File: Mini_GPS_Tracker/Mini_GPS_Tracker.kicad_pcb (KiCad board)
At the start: 4 copper layers, 38.1 x 99.1 mm, 56 parts, among them J1 USB_C_Receptacle, J2 Screw_Terminal_01x02, J3 901-10512-1, J4 Conn_ARM_JTAG_SWD_10, SW1 SW_Push, SW2 MLL1200S, U1 CH340E, U2 MS5611-01BA, U3 LD1117S33TR_SOT223, U4 MAX-8Q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

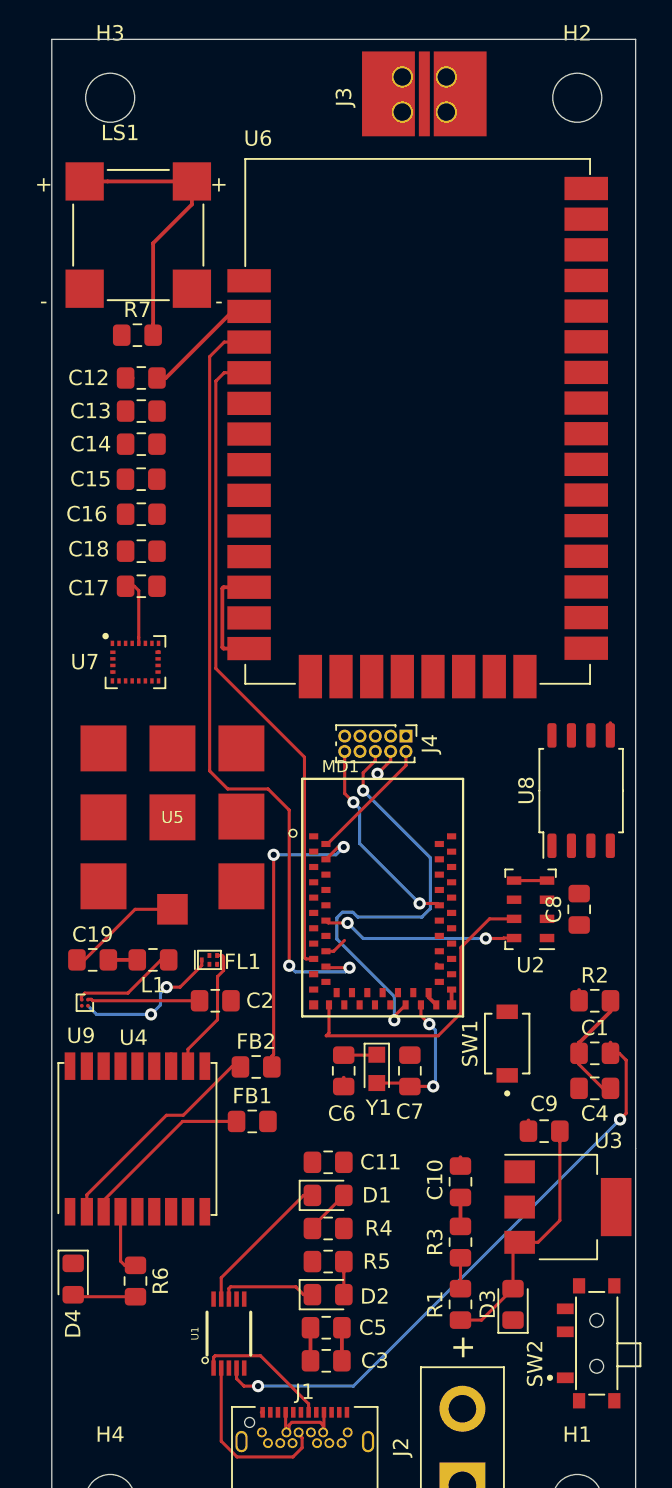
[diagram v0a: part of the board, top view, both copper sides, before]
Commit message: all  artemis connections routed
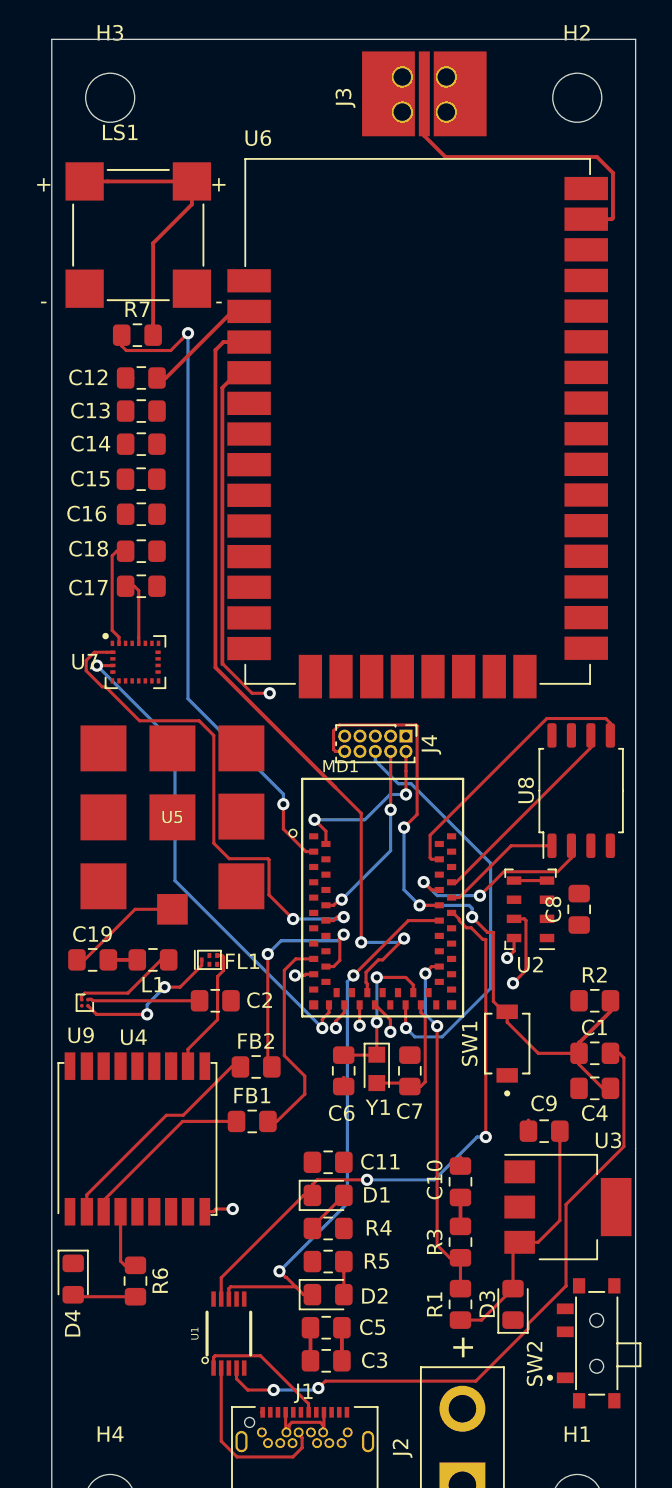
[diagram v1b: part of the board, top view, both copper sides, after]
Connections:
- MD1 pad 11: cs_flash -> Net-(MD1-Pad11)
- MD1 pad 12: Pressure_SCL -> 9_SCL
- MD1 pad 13: clk_flash -> Net-(MD1-Pad13)
- MD1 pad 16: buzzer -> Net-(MD1-Pad16)
- MD1 pad 17: TRANS_RX -> GPS_RX
- MD1 pad 18: TRANS_TX -> GPS_TX
- MD1 pad 19: Net-(MD1-Pad19) -> Pressure_SCL
- MD1 pad 23: Pressure_SDA -> 9_SDA
- MD1 pad 25: Net-(MD1-Pad25) -> Pressure_SDA
- MD1 pad 27: Net-(MD1-Pad27) -> TRANS_RX
- MD1 pad 28: Net-(MD1-Pad28) -> TRANS_TX
- MD1 pad 29: Net-(MD1-Pad29) -> gps_reset
- MD1 pad 3: Net-(MD1-Pad3) -> buzzer
- MD1 pad 4: GPS_TX -> Net-(MD1-Pad4)
- MD1 pad 51: Net-(MD1-Pad51) -> cs_flash
- MD1 pad 52: 9_SDA -> MISO_Flash
- MD1 pad 53: 9_SCL -> clk_flash
- MD1 pad 56: GPS_RX -> MOSI_Flash
- MD1 pad 58: gps_reset -> Net-(MD1-Pad58)
- MD1 pad 6: MISO_Flash -> Net-(MD1-Pad6)
- MD1 pad 8: MOSI_Flash -> Net-(MD1-Pad8)
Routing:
- net buzzer: track 1.50 -> 43.1 mm, vias 0 -> 2
- net 9_SCL: track 0.00 -> 32.9 mm, vias 0 -> 2
- net 9_SDA: track 0.00 -> 32.5 mm, vias 0 -> 2
- net RXI: track 6.40 -> 36.3 mm, vias 0 -> 2
- net TX0: track 9.57 -> 38.8 mm, vias 0 -> 2
- net RESET: track 21.2 -> 47.1 mm, vias 2 -> 3
- net v_measure: track 2.27 -> 23.0 mm, vias 0 -> 2
- net Net-(J3-Pad1): track 0.00 -> 20.8 mm
- net gps_reset: track 0.10 -> 19.9 mm, vias 0 -> 2
- net MOSI_Flash: track 0.80 -> 18.1 mm
- net GPS_RX: track 0.10 -> 14.0 mm
- net clk_flash: track 0.00 -> 13.5 mm
- net MISO_Flash: track 0.10 -> 13.1 mm, vias 0 -> 2
- net SWDCK: track 1.88 -> 12.3 mm, vias 1 -> 2
- net GND: track 23.4 -> 15.0 mm
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- removed copper zone on PWR, net +3V3
- removed copper zone on GND, net GND

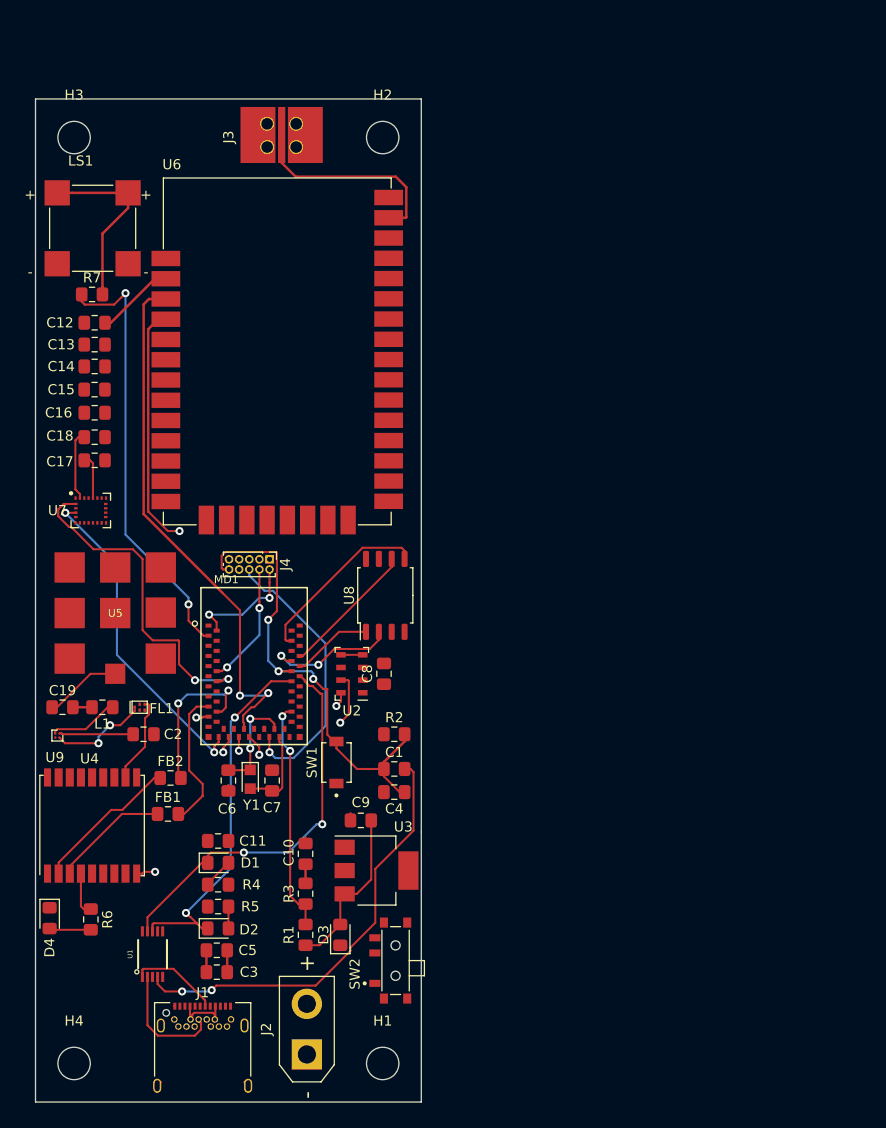
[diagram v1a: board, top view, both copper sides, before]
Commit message: all tracks routed
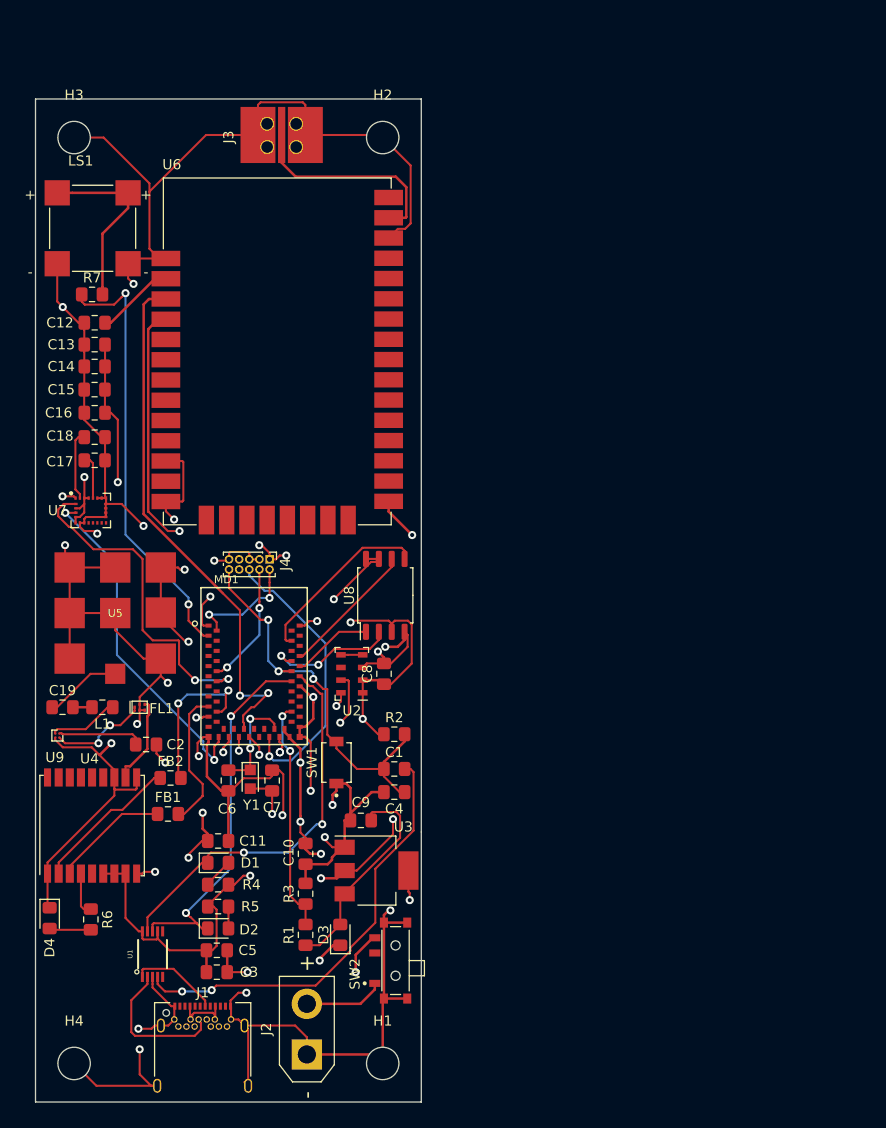
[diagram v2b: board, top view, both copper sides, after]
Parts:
- moved C2 1.05 mm to (158.2, 104.4)
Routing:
- net GND: track 15.0 -> 457.5 mm, vias 0 -> 28
- net +3V3: track 4.05 -> 201.0 mm, vias 0 -> 18
- net Net-(D3-Pad1): track 0.00 -> 11.1 mm, vias 0 -> 2
- net Net-(J2-Pad2): track 0.00 -> 7.90 mm
- net RESET: track 47.1 -> 39.5 mm
- net Net-(C9-Pad1): track 16.5 -> 21.2 mm
- net Net-(C7-Pad1): track 8.53 -> 12.8 mm, vias 0 -> 3
- net Net-(J1-PadB7): track 12.0 -> 14.6 mm
- net 9_SDA: track 32.5 -> 34.0 mm
- net Net-(C2-Pad1): track 7.27 -> 8.35 mm
- net A1: track 27.7 -> 28.3 mm
